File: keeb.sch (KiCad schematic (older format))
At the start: 155 parts, among them J1 AudioJack3, J101 USB_C_Receptacle_USB2.0, J102 AVR-ISP-6, SW101 SW_Push, SW102 SW_Push, SW103 SW_Push, SW104 SW_Push, SW105 SW_Push, SW106 SW_Push, SW107 SW_Push, SW108 SW_Push, SW109 SW_Push, SW110 SW_Push, SW111 SW_Push, SW112 SW_Push, SW113 SW_Push, SW114 SW_Push, SW115 SW_Push, SW116 SW_Push, SW117 SW_Push, SW118 SW_Push, SW119 SW_Push, SW120 SW_Push, SW121 SW_Push, SW122 SW_Push, SW123 SW_Push, SW124 SW_Push, SW125 SW_Push, SW126 SW_Push, SW127 SW_Push, SW128 SW_Push, SW129 SW_Push, SW130 SW_Push, SW131 SW_Push, SW132 SW_Push, SW133 SW_Push, SW134 SW_Push, SW135 SW_Push, SW136 SW_Push, SW137 SW_Push, SW138 SW_Push, SW139 SW_Push, SW140 SW_Push, SW141 SW_Push, SW142 SW_Push, SW143 SW_Push, SW144 SW_Push, SW145 SW_Push, SW146 SW_Push, SW147 SW_Push, SW148 SW_Push, SW149 SW_Push, SW150 SW_Push, SW151 SW_Push, SW152 SW_Push, SW153 SW_Push, SW154 SW_Push, SW155 SW_Push, SW156 SW_Push, SW157 SW_Push, SW158 SW_Push, SW159 SW_Push, SW160 SW_Push, SW161 SW_Push, SW162 SW_Push, SW163 SW_Push, SW164 SW_Push, SW165 SW_Push, SW166 SW_Push, SW167 SW_Push, U102 ATmega32U4-AU, Y1 16Mhz

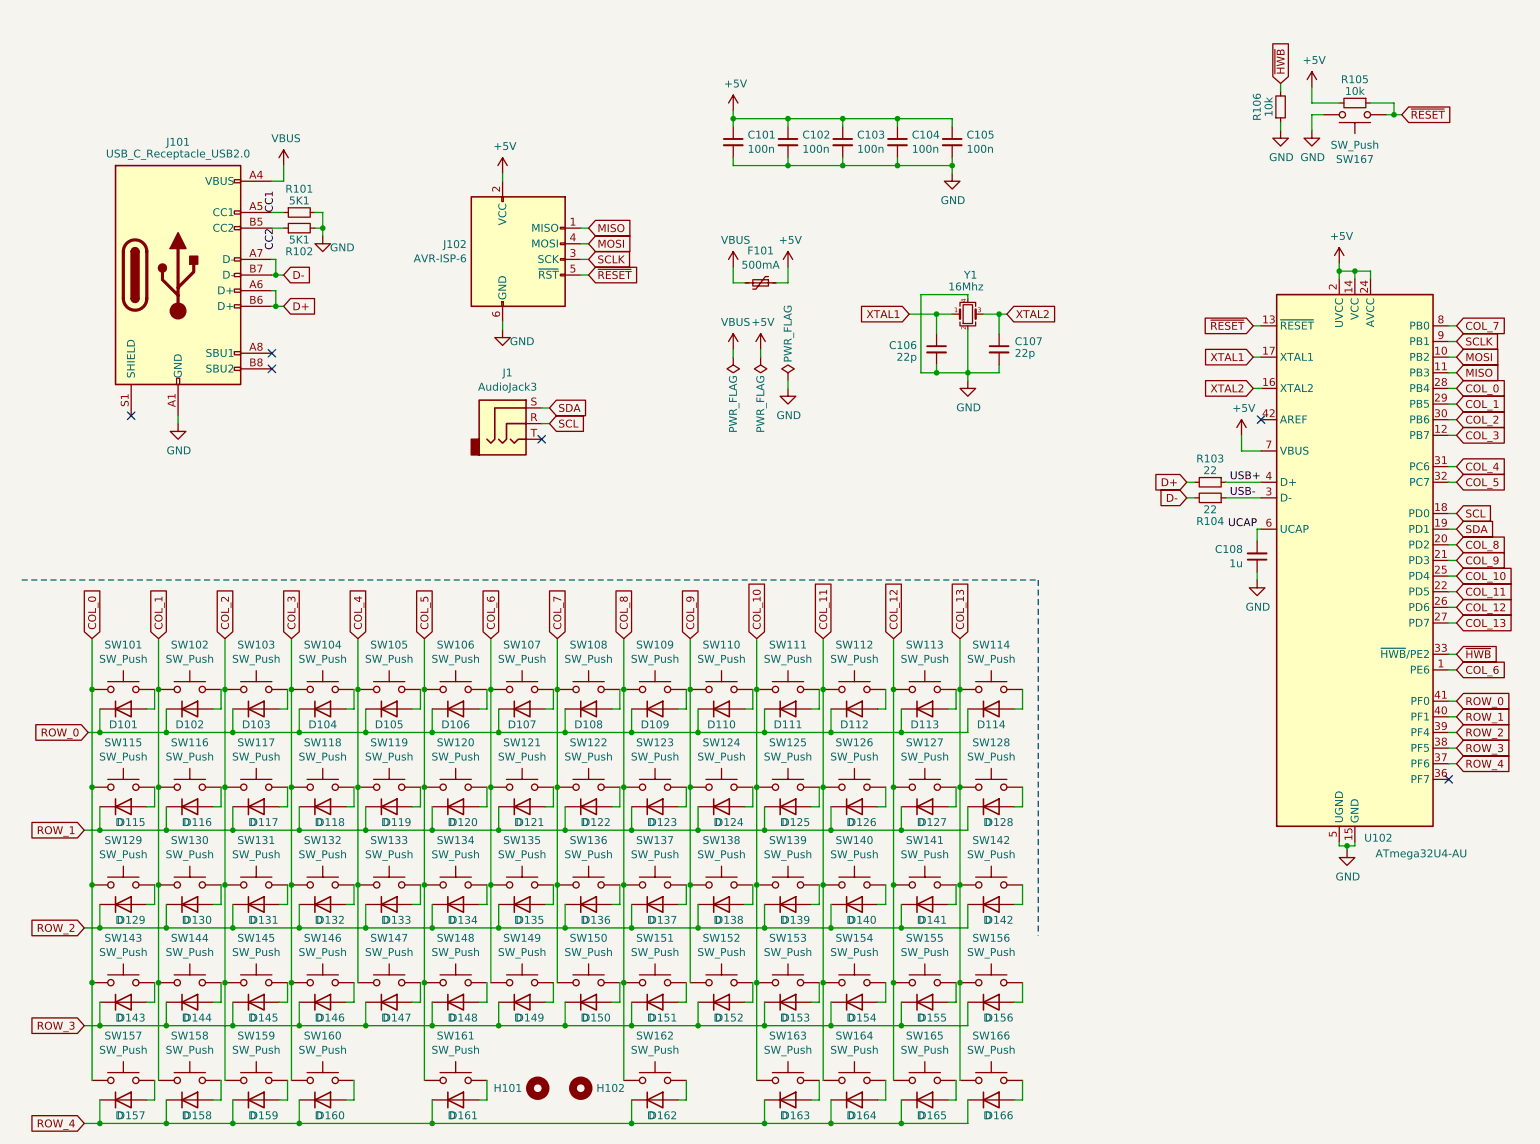
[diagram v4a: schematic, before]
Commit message: first pass layout complete
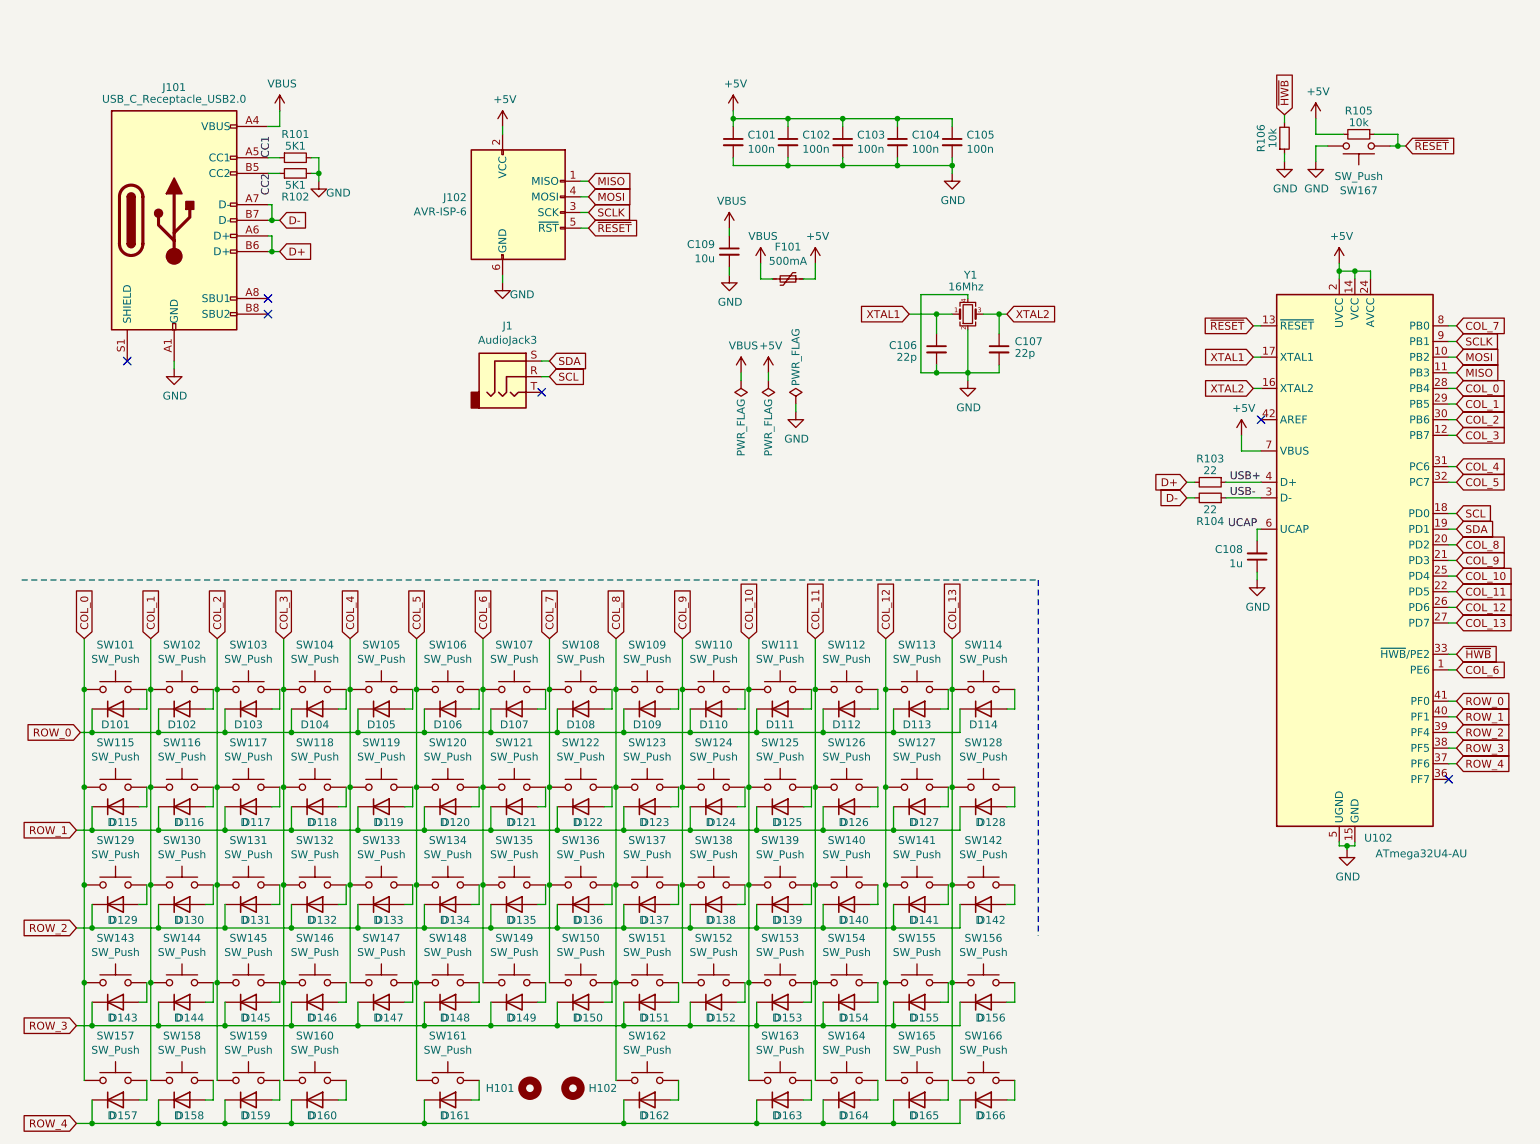
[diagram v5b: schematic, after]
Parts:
- added C109: 10u, Capacitor_SMD:C_1206_3216Metric_Pad1.33x1.80mm_HandSolder, symbol Device:C_Small
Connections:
- net GND: now also C109.2
- net VBUS: now also C109.1
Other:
- moved on the sheet: D101, D102, D103, D104, D105, D106, D107, D108, D109, D110, D111, D112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

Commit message: lp rst sw
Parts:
- SW167: footprint Button_Switch_THT:SW_PUSH_6mm_H5mm -> Button_Switch_SMD:SW_SPST_B3U-1000P
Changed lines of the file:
@@
 F 0 "SW167" H 9025 1760 50  0000 C CNN
 F 1 "SW_Push" H 9025 1669 50  0000 C CNN
-F 2 "Button_Switch_THT:SW_PUSH_6mm_H5mm" H 9025 1675 50  0001 C CNN
+F 2 "Button_Switch_SMD:SW_SPST_B3U-1000P" H 9025 1675 50  0001 C CNN
 F 3 "~" H 9025 1675 50  0001 C CNN
 	1    9025 1475
